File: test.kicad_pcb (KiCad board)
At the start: 2 copper layers, 20 parts, among them J1 Conn_01x04_Pin, J2 XT90PW-F, J3 XT90PW-F, Q1 S8550 2TY DNP SOT-23 SMD 0.5A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, U1 LM741, U3 HX711, U4 MPXV7002DP

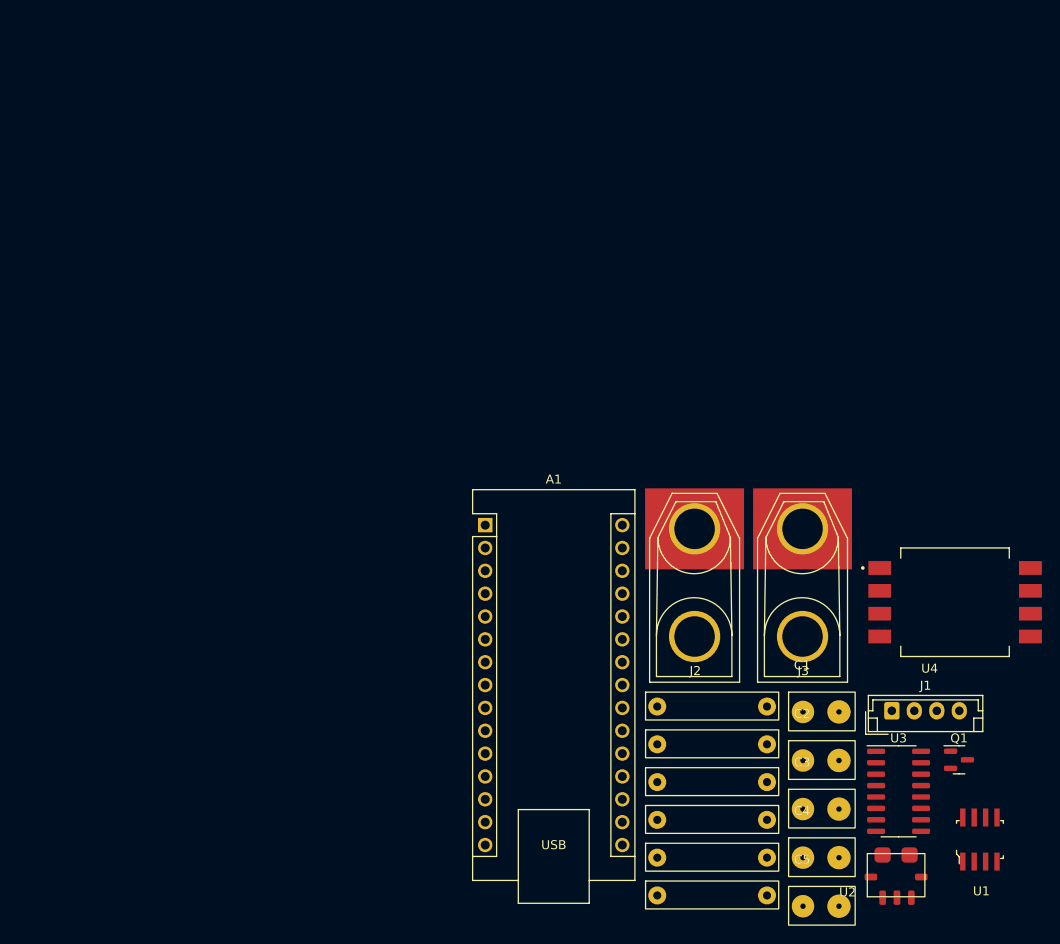
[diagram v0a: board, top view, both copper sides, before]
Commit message: Replaced test files
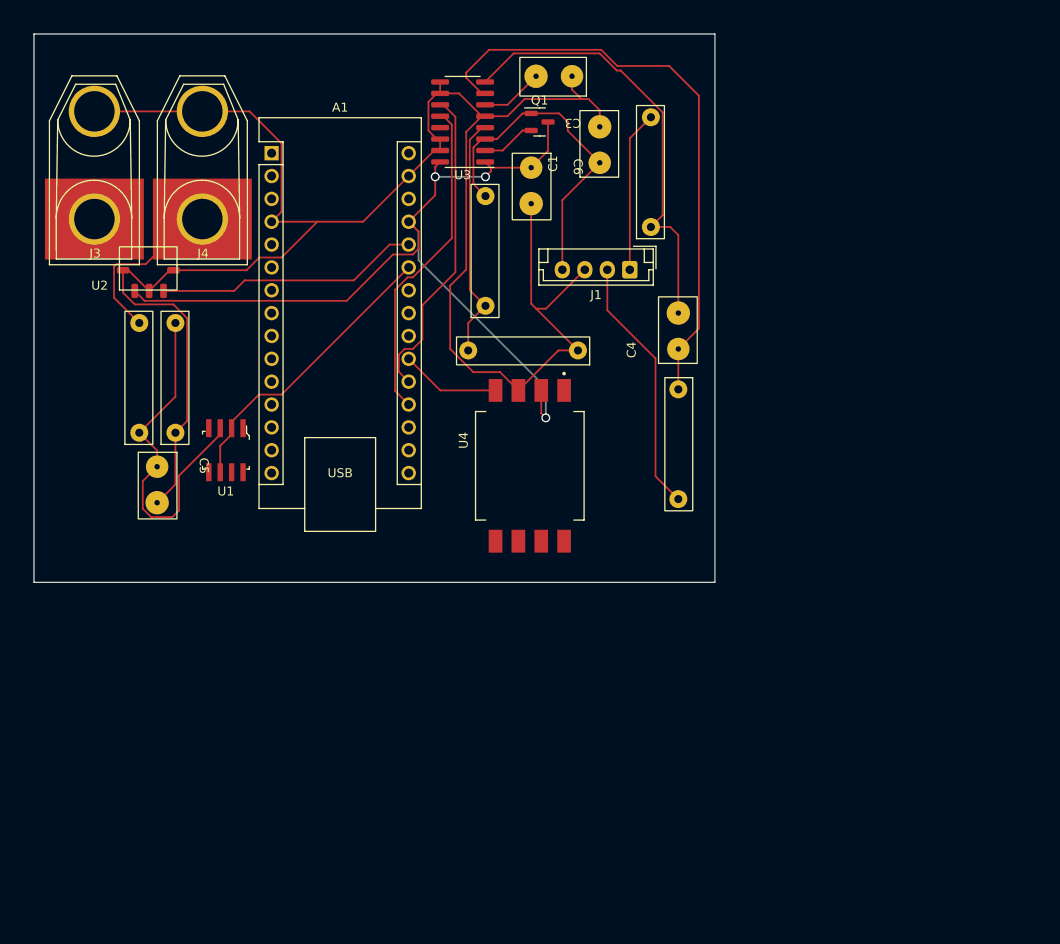
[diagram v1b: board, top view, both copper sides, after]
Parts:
- removed C2: 1u, Userlib:Capacitor_4mm_diam_.6mm_pin
- removed J2: XT90PW-F, Userlib:XT90_-F
- added C6: 10u, Userlib:Capacitor_4mm_diam_.6mm_pin, F.Cu at (150.8, 88.5)
- added J4: XT90PW-F, Userlib:XT90_-F, F.Cu at (114.3, 96.5)
- C4: value 10n -> 1u
- C5: value 10u -> 10n
- U1: footprint Userlib:LM741 -> digikey-footprints:SOIC-8_W3.9mm
- moved U2 107.1 mm to (105.0, 100.1)
- moved U1 97.5 mm to (116.8, 117.9), turned to 180 degrees
- moved J3 91.4 mm to (102.3, 96.5)
- moved U3 88.8 mm to (143.2, 81.4), turned to 180 degrees
- moved C5 87.4 mm to (109.2, 121.7), turned to -90 degrees
- moved C3 86.7 mm to (153.3, 76.3), turned to 180 degrees
- moved Q1 84.9 mm to (151.7, 81.4)
- moved R2 74.3 mm to (107.2, 110.8), turned to 90 degrees
- moved R3 73.4 mm to (111.2, 110.8), turned to 90 degrees
- moved R4 71.4 mm to (164.1, 87.9), turned to 90 degrees
- moved R5 70.8 mm to (145.7, 96.6), turned to 90 degrees
- moved C1 67.7 mm to (158.4, 83.9), turned to 90 degrees
- moved R6 63.6 mm to (150.8, 106.8), turned to 180 degrees
- moved C4 60.7 mm to (167.1, 104.6), turned to 90 degrees
- moved J1 57.0 mm to (161.7, 97.8), turned to 180 degrees
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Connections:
- C3 pad 1: Net-(U3-INA-) -> GND
- C3 pad 2: Net-(U3-INA+) -> Net-(U3-VBG)
- C4 pad 1: Net-(U1-+) -> Net-(U3-INA-)
- C4 pad 2: GND -> Net-(U3-INA+)
- C5 pad 1: Net-(A1-+5V) -> Net-(U1-+)
- R2 pad 1: Net-(J3-Pos) -> Net-(J4-Pos)
- U2 pad 5: Net-(J3-Pos) -> Net-(J4-Pos)
- U2 pad 6: Net-(J2-Pos) -> Net-(J3-Pos)
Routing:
- net GND: track 0.00 -> 216.9 mm
- net Net-(A1-+5V): track 0.00 -> 95.8 mm, vias 0 -> 3
- net Net-(U3-INA-): track 0.00 -> 66.0 mm
- net Net-(U3-INA+): track 0.00 -> 49.1 mm
- net Net-(U1-+): track 0.00 -> 40.3 mm
- net Net-(J1-Pin_4): track 0.00 -> 38.0 mm
- net Net-(A1-A0): track 0.00 -> 36.4 mm
- net Net-(A1-A1): track 0.00 -> 35.3 mm
- net Net-(A1-A6): track 0.00 -> 32.9 mm
- net Net-(A1-A7): track 0.00 -> 29.4 mm
- net Net-(J1-Pin_2): track 0.00 -> 28.8 mm
- net Net-(U3-VFB): track 0.00 -> 27.2 mm
- net Net-(J1-Pin_1): track 0.00 -> 17.9 mm
- net Net-(J4-Pos): track 0.00 -> 13.6 mm
- net Net-(A1-A2): track 0.00 -> 11.1 mm
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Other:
- board outline added: 75.7 x 61 mm

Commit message: Raymond fixed nets and added SD card module
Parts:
- added J2: Conn_01x06, Connector_JST:JST_EH_B6B-EH-A_1x06_P2.50mm_Vertical, F.Cu at (134.6, 76.2)
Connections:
- A1 pad 17: unconnected-(A1-3V3-Pad17) -> Net-(A1-3V3)
- A1 pad 5: unconnected-(A1-D2-Pad5) -> Net-(A1-D2)
- A1 pad 6: unconnected-(A1-D3-Pad6) -> Net-(A1-D3)
- A1 pad 7: unconnected-(A1-D4-Pad7) -> Net-(A1-D4)
- A1 pad 8: unconnected-(A1-D5-Pad8) -> Net-(A1-D5)
- U2 pad 1: Net-(A1-+5V) -> Net-(A1-3V3)
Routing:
- net Net-(A1-3V3): track 0.00 -> 61.1 mm
- net Net-(A1-D5): track 0.00 -> 31.7 mm
- net Net-(A1-D4): track 0.00 -> 28.1 mm
- net Net-(A1-D3): track 0.00 -> 24.6 mm
- net Net-(A1-D2): track 0.00 -> 21.0 mm
- net Net-(A1-+5V): track 95.8 -> 81.0 mm, vias 3 -> 4
- added copper zone on B.Cu, net GND

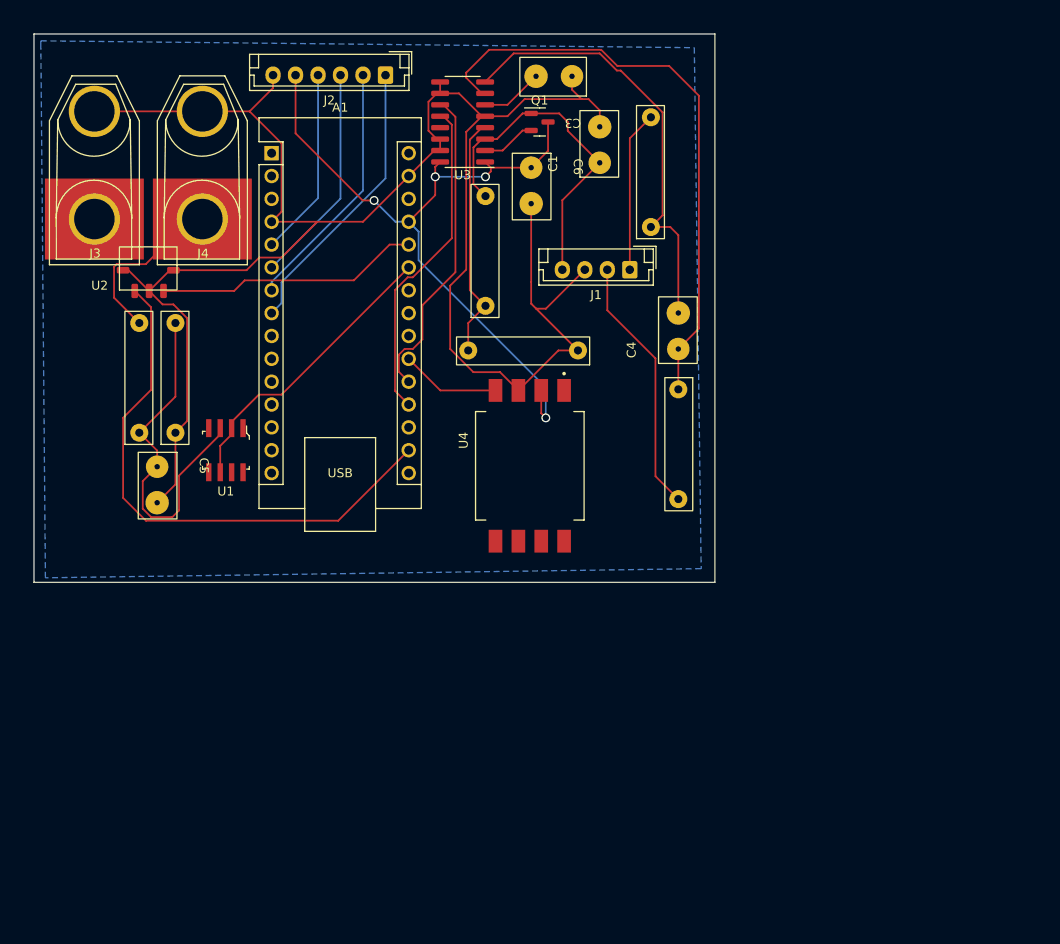
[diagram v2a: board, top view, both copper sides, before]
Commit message: Fixed the SD Card
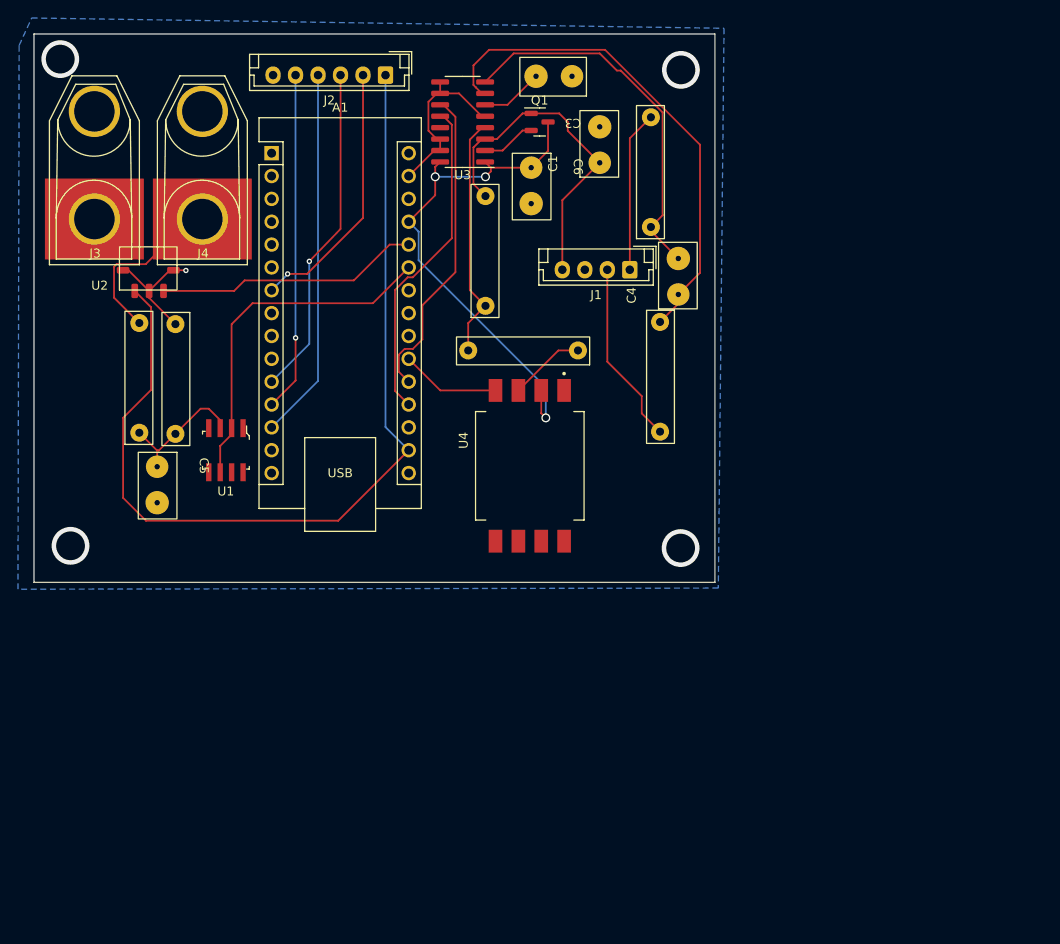
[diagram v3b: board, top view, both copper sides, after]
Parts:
- moved R1 7.76 mm to (165.1, 108.8)
- moved C4 6.06 mm to (167.1, 98.6)
- moved R3 1.67 mm to (111.2, 109.1), turned to -90 degrees
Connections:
- A1 pad 11: unconnected-(A1-D8-Pad11) -> Net-(A1-D8)
- A1 pad 12: unconnected-(A1-D9-Pad12) -> Net-(A1-D9)
- A1 pad 13: unconnected-(A1-D10-Pad13) -> Net-(A1-D10)
- A1 pad 5: Net-(A1-D2) -> unconnected-(A1-D2-Pad5)
- A1 pad 6: Net-(A1-D3) -> unconnected-(A1-D3-Pad6)
- A1 pad 8: Net-(A1-D5) -> unconnected-(A1-D5-Pad8)
- J2 pad 1: Net-(A1-D5) -> Net-(A1-3V3)
- J2 pad 3: Net-(A1-D3) -> Net-(A1-D8)
- J2 pad 4: Net-(A1-D2) -> Net-(A1-D10)
- J2 pad 5: Net-(A1-+5V) -> Net-(A1-D9)
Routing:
- net GND: track 216.7 -> 42.2 mm, vias 0 -> 1
- net Net-(A1-3V3): track 61.1 -> 103.8 mm
- net Net-(A1-D10): track 0.00 -> 41.3 mm
- net Net-(A1-D9): track 0.00 -> 37.8 mm, vias 0 -> 1
- net Net-(A1-D8): track 0.00 -> 37.3 mm, vias 0 -> 1
- net Net-(A1-D5): track 31.7 -> 0.00 mm
- net Net-(U1-+): track 40.3 -> 15.7 mm
- net Net-(A1-D3): track 24.6 -> 0.00 mm
- net Net-(A1-+5V): track 81.0 -> 57.6 mm, vias 4 -> 3
- net Net-(A1-D2): track 21.0 -> 0.00 mm
- net Net-(U3-INA-): track 66.0 -> 55.7 mm
- net Net-(J1-Pin_2): track 28.8 -> 20.4 mm
- net Net-(U3-INA+): track 49.1 -> 41.8 mm
- net Net-(A1-A6): track 32.9 -> 39.3 mm
- net Net-(A1-D4): track 28.1 -> 29.4 mm, vias 0 -> 1
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
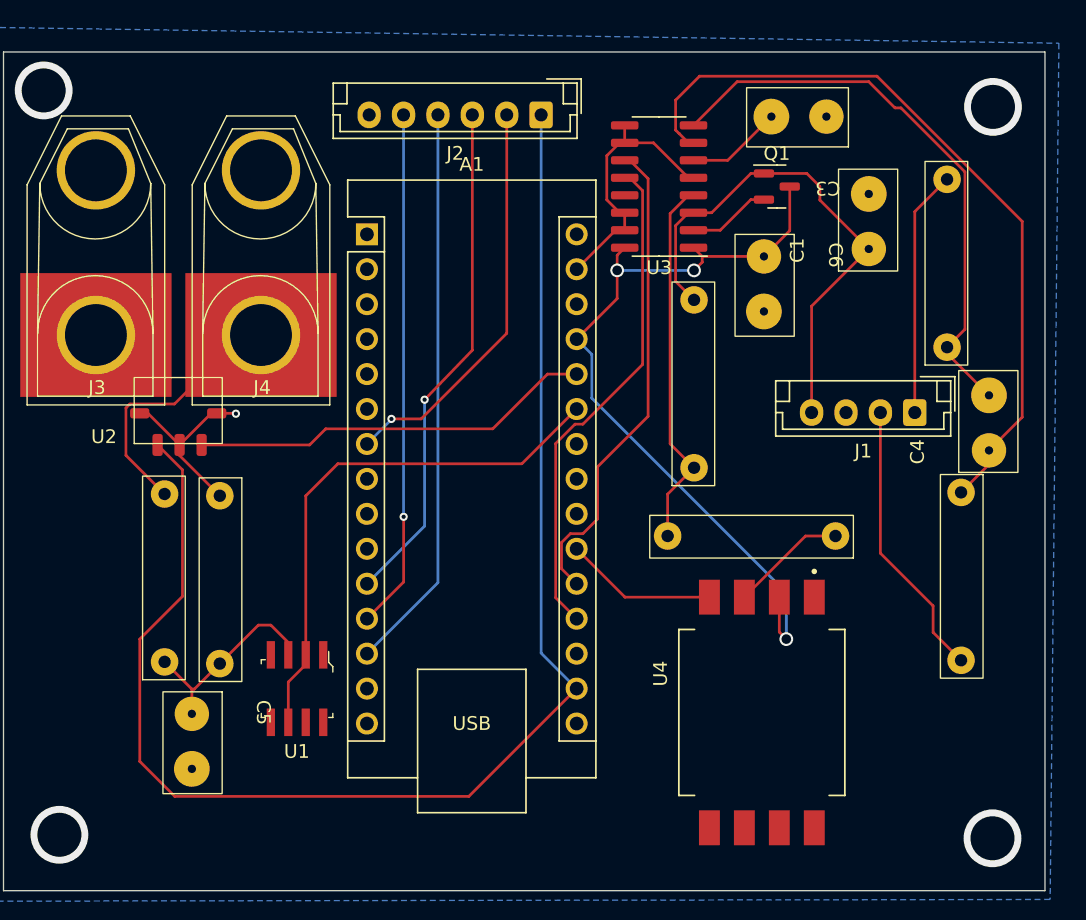
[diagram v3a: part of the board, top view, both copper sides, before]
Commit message: added labels to PCB
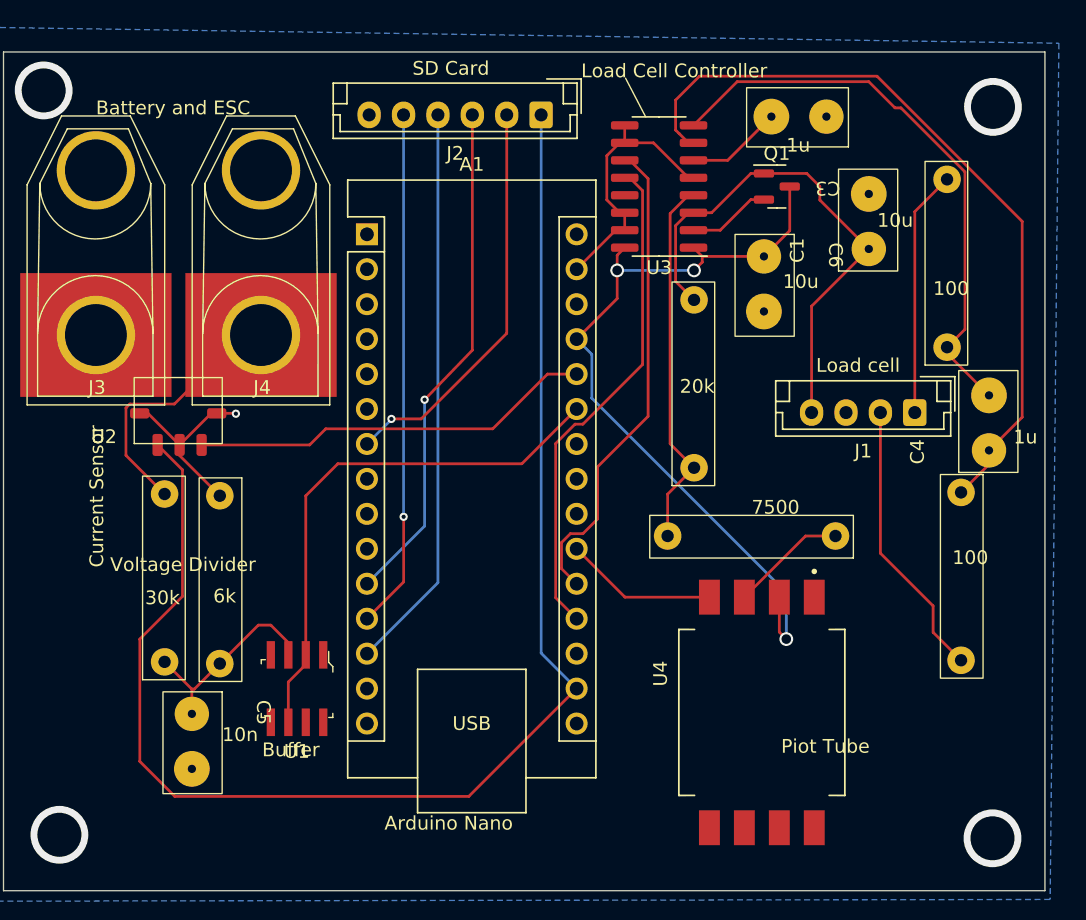
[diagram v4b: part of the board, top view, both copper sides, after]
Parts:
- J2: value Conn_01x06 -> SD Card
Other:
- board text added: "100"
- board text added: "10n"
- board text added: "10u"
- board text added: "1u"
- board text added: "20k"
- board text added: "30k"
- board text added: "6k"
- board text added: "7500"
- board text added: "Arduino Nano"
- board text added: "Battery and ESC"
- board text added: "Buffer"
- board text added: "Current Sensor"
- board text added: "DBF UTD"
- board text added: "Load Cell Controller"
- board text added: "Load cell"
- board text added: "Piot Tube"
- board text added: "SD Card"
- board text added: "Voltage Divider"
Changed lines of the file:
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@@
         (effects (font (size 1 1) (thickness 0.15)))
     )
-    (fp_text value "Conn_01x06" (at 6.25 3.4) (layer "F.Fab")
+    (fp_text value "SD Card" (at 6.25 3.4) (layer "F.Fab")
         (effects (font (size 1 1) (thickness 0.15)))
     )
@@
       (net 4 "GND") (pintype "passive"))
   )
+  (gr_line (start 140.716 73.533) (end 142.179396 76.347)
+    (stroke (width 0.1) (type default)) (layer "F.SilkS"))
   (gr_rect (start 95.504 71.628) (end 171.196 132.588)
     (stroke (width 0.05) (type default)) (fill none) (layer "Edge.Cuts"))
+  (gr_text "DBF UTD" (at 168.529 128.524) (layer "B.SilkS")
+    (effects (font (size 10 10) (thickness 0.2)) (justify left bottom mirror))
+  )
+  (gr_text "Buffer" (at 114.3 122.936) (layer "F.SilkS")
+    (effects (font (size 1 1) (thickness 0.1)) (justify left bottom))
+  )
+  (gr_text "20k" (at 144.653 96.52) (layer "F.SilkS")
+    (effects (font (size 1 1) (thickness 0.1)) (justify left bottom))
+  )
+  (gr_text "6k" (at 110.744 111.76) (layer "F.SilkS")
+    (effects (font (size 1 1) (thickness 0.1)) (justify left bottom))
+  )
+  (gr_text "Load cell" (at 154.559 94.996) (layer "F.SilkS")
+    (effects (font (size 1 1) (thickness 0.1)) (justify left bottom))
+  )
+  (gr_text "7500" (at 149.874396 105.307) (layer "F.SilkS")
+    (effects (font (size 1 1) (thickness 0.1)) (justify left bottom))
+  )
+  (gr_text "1u" (at 168.91 100.203) (layer "F.SilkS")
+    (effects (font (size 1 1) (thickness 0.1)) (justify left bottom))
+  )
+  (gr_text "Current Sensor" (at 102.87 109.093 90) (layer "F.SilkS")
+    (effects (font (size 1 1) (thickness 0.1)) (justify left bottom))
+  )
+  (gr_text "1u" (at 152.4 78.994) (layer "F.SilkS")
+    (effects (font (size 1 1) (thickness 0.1)) (justify left bottom))
+  )
+  (gr_text "Load Cell Controller" (at 137.49 73.59) (layer "F.SilkS")
+    (effects (font (size 1 1) (thickness 0.1)) (justify left bottom))
+  )
+  (gr_text "Voltage Divider" (at 103.251 109.474) (layer "F.SilkS")
+    (effects (font (size 1 1) (thickness 0.1)) (justify left bottom))
+  )
+  (gr_text "SD Card" (at 125.222 73.406) (layer "F.SilkS")
+    (effects (font (size 1 1) (thickness 0.1)) (justify left bottom))
+  )
+  (gr_text "Arduino Nano" (at 123.19 128.27) (layer "F.SilkS")
+    (effects (font (size 1 1) (thickness 0.1)) (justify left bottom))
+  )
+  (gr_text "100" (at 164.465 108.966) (layer "F.SilkS")
+    (effects (font (size 1 1) (thickness 0.1)) (justify left bottom))
+  )
+  (gr_text "100" (at 163.068 89.408) (layer "F.SilkS")
+    (effects (font (size 1 1) (thickness 0.1)) (justify left bottom))
+  )
+  (gr_text "Battery and ESC" (at 102.22 76.28) (layer "F.SilkS")
+    (effects (font (size 1 1) (thickness 0.1)) (justify left bottom))
+  )
+  (gr_text "30k" (at 105.791 111.887) (layer "F.SilkS")
+    (effects (font (size 1 1) (thickness 0.1)) (justify left bottom))
+  )
+  (gr_text "Piot Tube" (at 152.019 122.682) (layer "F.SilkS")
+    (effects (font (size 1 1) (thickness 0.1)) (justify left bottom))
+  )
+  (gr_text "10u" (at 159.004 84.455) (layer "F.SilkS")
+    (effects (font (size 1 1) (thickness 0.1)) (justify left bottom))
+  )
+  (gr_text "10u" (at 152.146 88.9) (layer "F.SilkS")
+    (effects (font (size 1 1) (thickness 0.1)) (justify left bottom))
+  )
+  (gr_text "10n" (at 111.395 121.833) (layer "F.SilkS")
+    (effects (font (size 1 1) (thickness 0.1)) (justify left bottom))
+  )
   (via (at 167.420942 75.619358) (size 4.2) (drill 3.2) (layers "F.Cu" "B.Cu") (free) (net 0))
   (via (at 167.386 128.778) (size 4.2) (drill 3.2) (layers "F.Cu" "B.Cu") (free) (net 0))

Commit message: Fixed caps and generated the gerber and drill files
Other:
- board text added: ".1u"
- board text added: "Pitot Tube"
- board text removed: "1u"
- board text removed: "Piot Tube"
